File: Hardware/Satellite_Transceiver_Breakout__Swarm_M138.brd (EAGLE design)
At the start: 35.6 x 88.9 mm, 97 parts, among them Q2 20V/4.2A/52mΩ/1.4W, Q4 20V/4.2A/52mΩ/1.4W, U1 CH340E_MSOP10, U2 SWARM_M138_TRANSCEIVER_MAIN, U3 STLQ015-3.3V

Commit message: Replace 3.3V Reg with AP2112K
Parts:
- U3: value STLQ015-3.3V -> 3.3V
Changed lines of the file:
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@@
 <attribute name="VALUE" x="17.78" y="25.781" size="0.762" layer="27" align="center"/>
 </element>
-<element name="U3" library="SparkFun-IC-Power" package="SOT23-5" value="STLQ015-3.3V" x="5.08" y="8.255" smashed="yes" rot="R90">
+<element name="U3" library="SparkFun-IC-Power" package="SOT23-5" value="3.3V" x="5.08" y="8.255" smashed="yes" rot="R90">
 <attribute name="NAME" x="2.921" y="6.477" size="0.6096" layer="25" ratio="20" rot="R90"/>
-<attribute name="PROD_ID" value="IC-15779" x="5.08" y="8.255" size="1.778" layer="27" ratio="15" rot="R90" display="off"/>
-<attribute name="VALUE" x="7.874" y="6.477" size="0.6096" layer="27" ratio="20" rot="R90"/>
+<attribute name="PROD_ID" value="VREG-12457" x="5.08" y="8.255" size="1.778" layer="27" ratio="15" rot="R90" display="off"/>
+<attribute name="VALUE" value="3.3V" x="7.874" y="6.477" size="0.6096" layer="27" ratio="20" rot="R90"/>
 </element>
 <element name="C8" library="SparkFun-Capacitors" package="0603" value="1.0uF" x="1.905" y="8.255" smashed="yes" rot="R90">

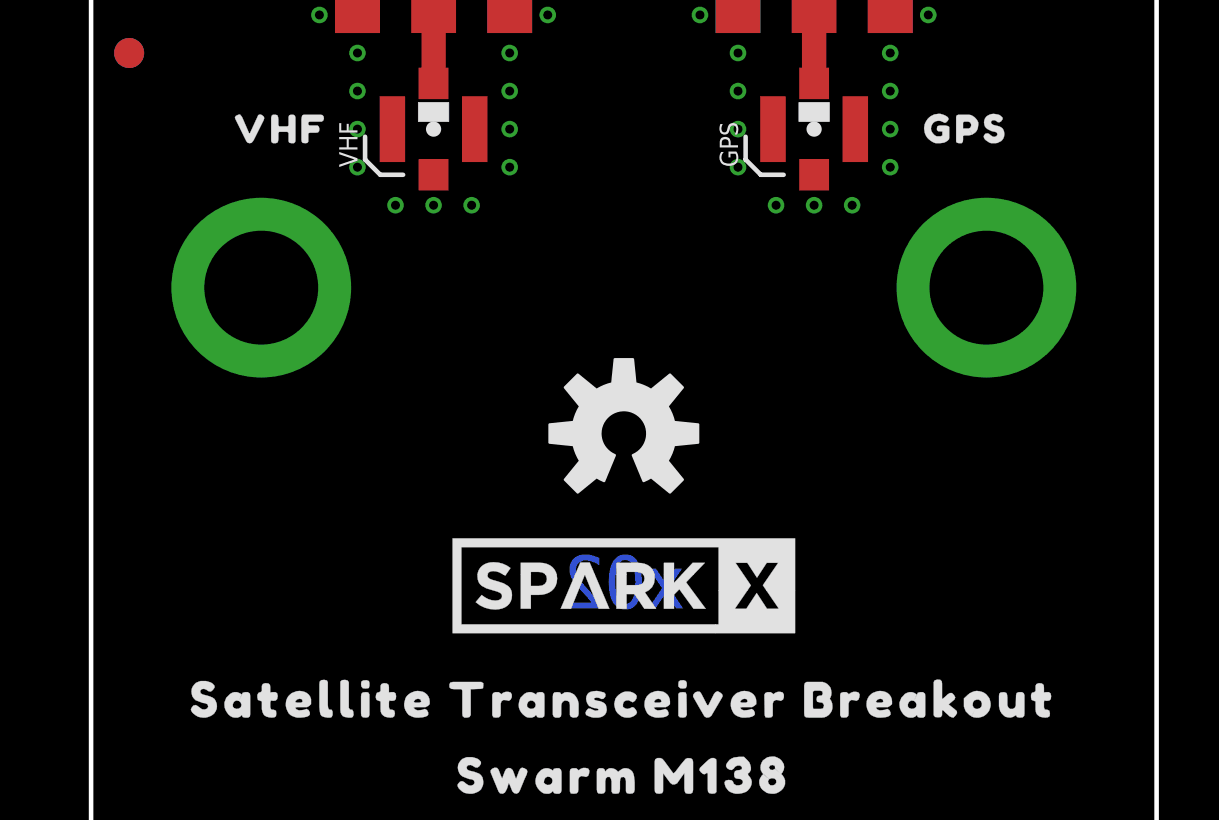
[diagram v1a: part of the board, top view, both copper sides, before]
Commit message: Updates for x03 PCB - move standoffs by 0.6mm and add route-out gaps in panel
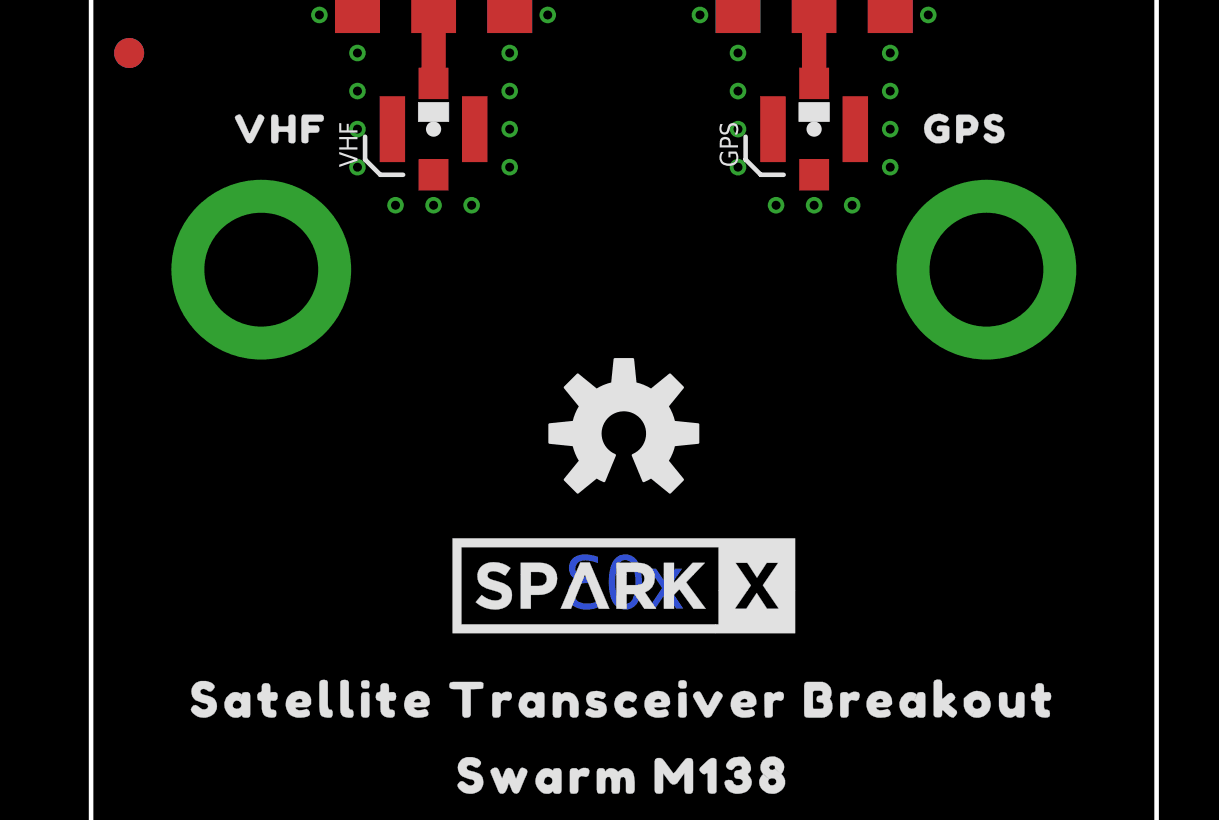
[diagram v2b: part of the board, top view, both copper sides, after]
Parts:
- U2: device Swarm:M.2-SWARM-M138-A -> SparkFun-RF:M.2-SWARM-M138-A
- moved H5 0.60 mm to (5.68, 75.3)
- moved H6 0.60 mm to (29.9, 75.3)
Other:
- board text added: "x03"
- board text removed: "x02"
